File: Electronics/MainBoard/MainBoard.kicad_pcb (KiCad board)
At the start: 2 copper layers, 25 parts, among them CN1 RCable_Con_Front, CN2 RCable_Con_Front, CN3 RCable_Con_VEST, M1 Vibr_Motor, Q1 Q_PNP_CBE, SW1 SW_PUSH, SW2 SPST, U1 LT1004_1.2V

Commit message: First implementation of the eclipse code, as well as some slight further changes to the electronics board.
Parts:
- added D3: D, Discret:R1, F.Cu at (123.2, 106.0)
- R1: value 50KΩ -> 47KΩ
- R2: value 14Ω -> 10Ω
- R7: value 68kΩ -> 47kΩ
- R8: value 33kΩ -> 22kΩ
- moved SP1 86.1 mm to (102.2, 83.2), turned to 0 degrees
- moved R4 63.8 mm to (72.4, 98.4)
- moved R3 63.6 mm to (72.4, 94.6)
- moved BT1 63.5 mm to (118.1, 111.1), turned to 180 degrees
- moved CN2 63.5 mm to (77.5, 87.0)
- moved Q1 63.5 mm to (72.4, 87.0)
- moved R5 63.5 mm to (72.4, 97.2)
- moved D1 62.3 mm to (67.3, 87.0)
- moved D2 62.3 mm to (67.3, 94.6)
- moved R2 59.7 mm to (71.1, 84.5)
- moved MCU1 52.9 mm to (116.8, 103.5), turned to 90 degrees
- moved SW2 52.7 mm to (122.6, 111.1), turned to 270 degrees
- moved CN1 50.8 mm to (109.2, 101.0)
- moved R6 49.3 mm to (118.1, 106.0), turned to 180 degrees
- moved U1 46.1 mm to (129.5, 90.8), turned to 0 degrees
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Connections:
- SW2 pad 1: Net-(BT1-Pad1) -> Net-(D3-Pad1)

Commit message: Adjusted electronics for new knowledge :3
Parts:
- removed R1: 47KΩ, Discret:R1
- removed U1: LT1004_1.2V, TO_SOT_Packages_THT:TO-92_Inline_Wide
- added C3: C, Capacitors_ThroughHole:CP_Radial_D5.0mm_P2.50mm, F.Cu at (134.6, 90.8)
- added J1: CONN_02X04, Pin_Headers:Pin_Header_Straight_2x04_Pitch2.54mm, F.Cu at (129.5, 85.7)
- added R10: RST, Resistors_ThroughHole:R_Axial_DIN0204_L3.6mm_D1.6mm_P2.54mm_Vertical, F.Cu at (127.0, 90.8)
- added R11: RST, Resistors_ThroughHole:R_Axial_DIN0204_L3.6mm_D1.6mm_P2.54mm_Vertical, F.Cu at (124.5, 93.3)
- added R9: RST, Resistors_ThroughHole:R_Axial_DIN0204_L3.6mm_D1.6mm_P2.54mm_Vertical, F.Cu at (129.2, 93.3)
- added REF**: R_1206, Resistors_SMD:R_1206, B.Cu at (121.4, 89.6)
- added REF**: R_1206, Resistors_SMD:R_1206, B.Cu at (118.8, 113.6)
- added REF**: R_1206, Resistors_SMD:R_1206, B.Cu at (117.1, 90.4)
- added REF**: R_1206, Resistors_SMD:R_1206, B.Cu at (125.6, 99.7)
- added REF**: R_1206, Resistors_SMD:R_1206, B.Cu at (118.3, 93.3)
- added REF**: R_1206, Resistors_SMD:R_1206, B.Cu at (125.9, 108.7)
- added REF**: R_1206, Resistors_SMD:R_1206, B.Cu at (118.2, 100.4)
- moved SP1 15.9 mm to (97.8, 98.4), turned to 270 degrees
- moved R8 10.2 mm to (141.0, 93.3)
- moved CN1 7.62 mm to (109.2, 93.3)
- moved D3 5.82 mm to (118.1, 108.8)
- moved R7 5.08 mm to (141.0, 90.8)
- moved SPI1 5.08 mm to (144.8, 93.3)
- moved CN3 3.59 mm to (154.9, 93.3)
- moved D1 3.17 mm to (67.3, 90.2)
- moved QRZ1 1.39 mm to (138.3, 107.1)
- moved BT1 1.27 mm to (116.8, 111.1), turned to 0 degrees
- moved R4 1.27 mm to (72.4, 99.7)
- moved C2 0.43 mm to (142.7, 111.2)
- turned M1 to 180 degrees
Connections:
- MCU1 pad 13: /IR_IN -> Net-(MCU1-Pad13)
- MCU1 pad 14: Net-(MCU1-Pad14) -> /IR_IN
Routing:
- net /SCL: track 0.00 -> 97.7 mm
- net +3V3: track 0.00 -> 83.1 mm
- net /SDA: track 0.00 -> 68.5 mm
- net /RESET: track 0.00 -> 45.4 mm
- net /BZR: track 0.00 -> 41.1 mm
- net /IR_LED: track 0.00 -> 39.7 mm
- net (no net): track 0.00 -> 35.3 mm
- net /TRG: track 0.00 -> 33.1 mm
- net GND: track 0.00 -> 24.9 mm
- net /IR_IN: track 0.00 -> 22.4 mm
- net Net-(J1-Pad5): track 0.00 -> 17.3 mm
- net /V_SENS: track 0.00 -> 16.2 mm
- net /G_LED: track 0.00 -> 15.9 mm
- net /B_LED: track 0.00 -> 14.9 mm
- net /SCK: track 0.00 -> 14.1 mm
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- added copper zone on B.Cu, net GND

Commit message: Small cleanup of schematic & footprint
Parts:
- removed CN1, CN2: RCable_Con_Front, Pin_Headers:Pin_Header_Straight_2x05
- C3: value C -> 22uF
- R3, R4, R5: value 470Ω -> 220Ω
- moved J1 5.68 mm to (134.6, 83.2), turned to 270 degrees
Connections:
- CN3 pad 4: Net-(CN3-Pad4) -> /MOSI
- CN3 pad 5: Net-(CN3-Pad5) -> /MISO
- CN3 pad 6: Net-(CN3-Pad6) -> /SCK
- D1 pad 2: Net-(D1-Pad2) -> +3V3
- D2 pad 2: Net-(CN2-Pad1) -> GND
- J1 pad 1: /SDA -> /E>A
- J1 pad 4: /SCL -> Net-(J1-Pad4)
- J1 pad 8: /HIT_REC -> /A>E
- MCU1 pad 2: /R_LED -> /E>A
- MCU1 pad 24: Net-(MCU1-Pad24) -> /R_MZL
- MCU1 pad 25: Net-(MCU1-Pad25) -> /G_MZL
- MCU1 pad 26: Net-(MCU1-Pad26) -> /B_MZL
- MCU1 pad 3: /G_LED -> /A>E
- MCU1 pad 4: /B_LED -> Net-(MCU1-Pad4)
- Q1 pad 1: Net-(CN2-Pad1) -> GND
- R3 pad 2: Net-(CN2-Pad4) -> /R_MZL
- R4 pad 2: Net-(CN2-Pad5) -> /G_MZL
- R5 pad 2: Net-(CN2-Pad6) -> /B_MZL
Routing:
- net +3V3: track 83.1 -> 108.8 mm
- net /E>A: track 0.00 -> 23.8 mm
- net /SDA: track 68.5 -> 44.9 mm
- net Net-(J1-Pad6): track 6.13 -> 26.8 mm
- net Net-(J1-Pad5): track 17.3 -> 1.19 mm
- net /G_LED: track 15.9 -> 0.00 mm
- net /A>E: track 0.00 -> 15.9 mm
- net /SCL: track 97.7 -> 82.1 mm
- net Net-(MCU1-Pad4): track 0.00 -> 14.9 mm
- net /B_LED: track 14.9 -> 0.00 mm
- net Net-(J1-Pad3): track 9.72 -> 21.2 mm
- net Net-(MCU1-Pad26): track 8.89 -> 0.00 mm
- net /B_MZL: track 0.00 -> 8.89 mm
- net GND: track 24.9 -> 16.1 mm
- net /R_LED: track 7.95 -> 0.00 mm
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- removed copper zone on B.Cu, net GND

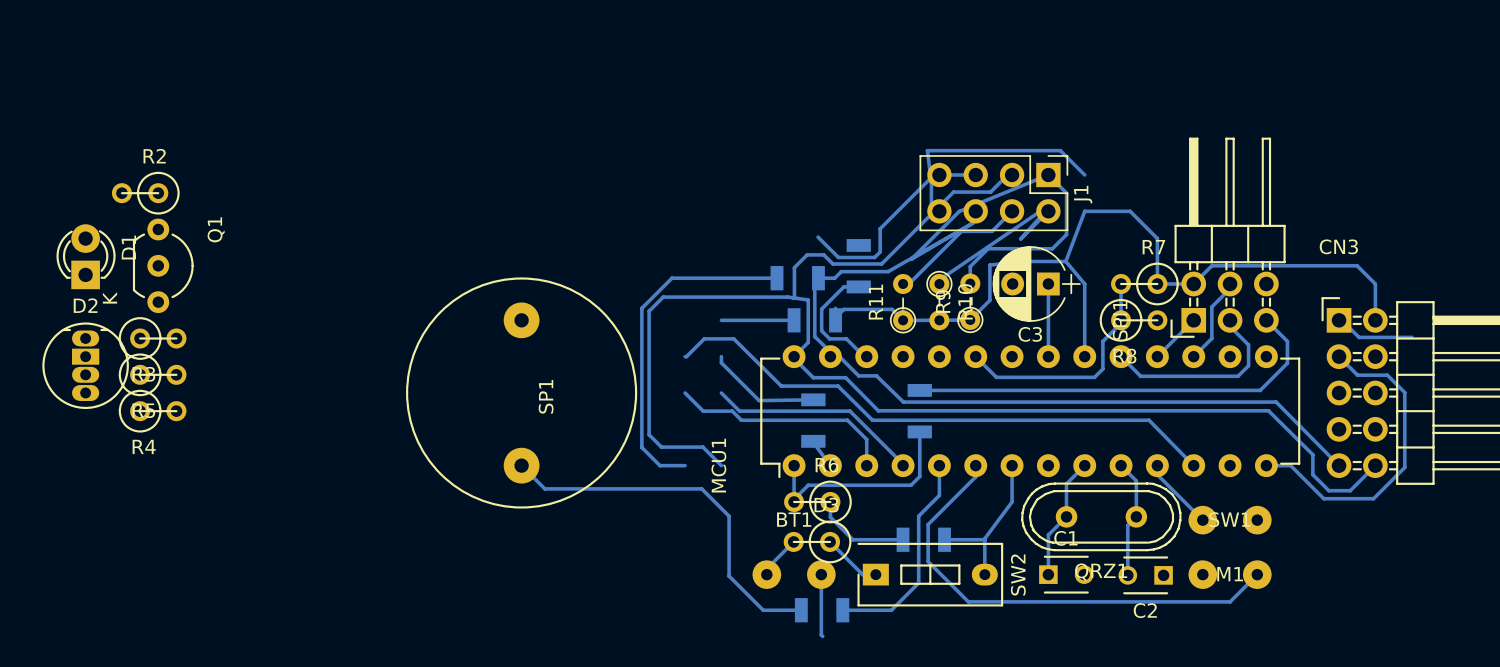
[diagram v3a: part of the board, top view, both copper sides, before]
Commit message: First implement of SMD components
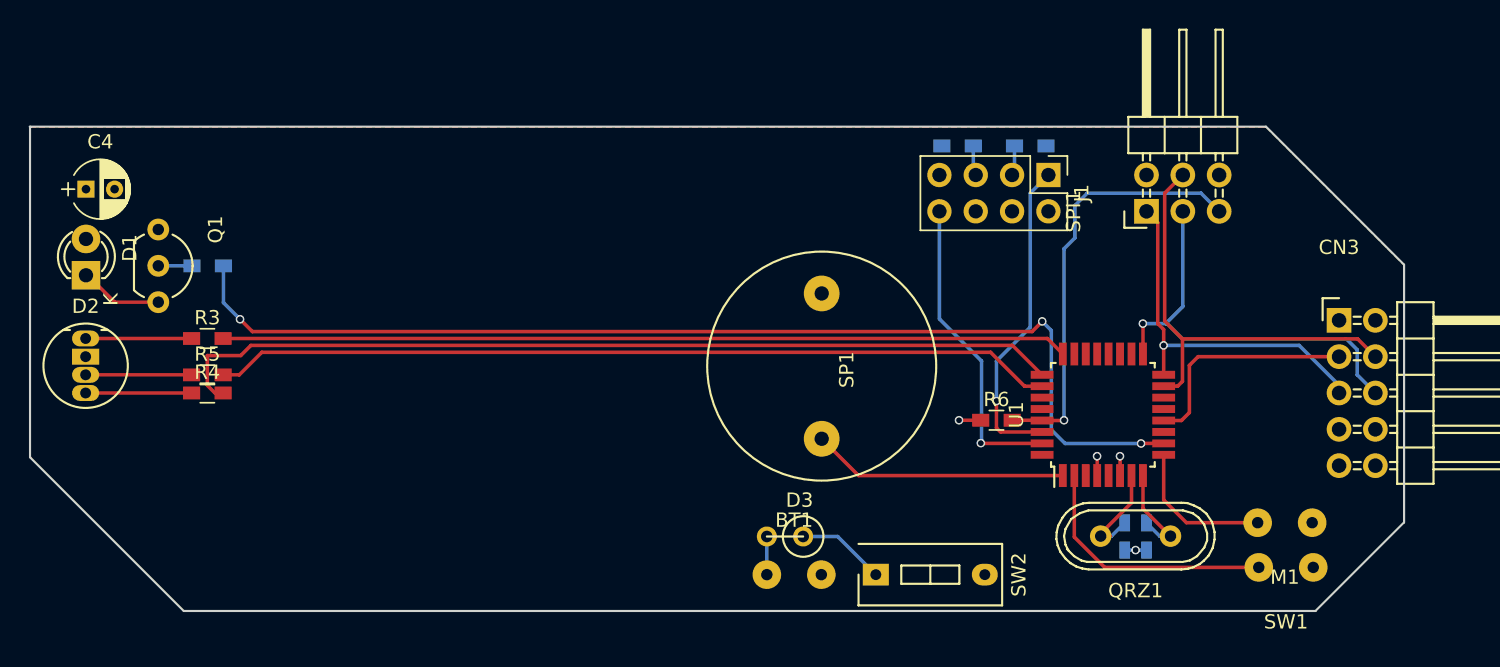
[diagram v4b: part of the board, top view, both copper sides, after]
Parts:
- removed C3: 22uF, Capacitors_ThroughHole:CP_Radial_D5.0mm_P2.50mm
- removed MCU1: ATMEGA328P-P, Housings_DIP:DIP-28_W7.62mm
- removed R10: RST, Resistors_ThroughHole:R_Axial_DIN0204_L3.6mm_D1.6mm_P2.54mm_Vertical
- removed R2: 10Ω, Discret:R1
- removed R7: 47kΩ, Discret:R1
- removed R8: 22kΩ, Discret:R1
- removed REF** (x7): R_1206, Resistors_SMD:R_1206
- added C4: CP, Capacitors_ThroughHole:CP_Radial_D4.0mm_P2.00mm, F.Cu at (67.3, 84.2)
- added R1: 220Ω, Resistors_SMD:R_0603_HandSoldering, B.Cu at (75.8, 89.5)
- added U1: ATMEGA168PA-AU, Housings_QFP:TQFP-32_7x7mm_Pitch0.8mm, F.Cu at (138.4, 99.9)
- C1, C2: footprint Capacitors_ThroughHole:C_Disc_D3_P2.5 -> Capacitors_SMD:C_0603_HandSoldering; moved to B.Cu
- R11, R9: footprint Resistors_ThroughHole:R_Axial_DIN0204_L3.6mm_D1.6mm_P2.54mm_Vertical -> Resistors_SMD:R_0603_HandSoldering; moved to B.Cu
- R3, R4, R5, R6: footprint Discret:R1 -> Resistors_SMD:R_0603_HandSoldering
- moved SP1 21.1 mm to (118.8, 96.5)
- moved R11 15.1 mm to (133.3, 81.2), turned to 180 degrees
- moved R6 14.1 mm to (131.0, 100.3), turned to 0 degrees
- moved R9 12.2 mm to (128.3, 81.2), turned to 0 degrees
- moved SPI1 8.30 mm to (141.5, 85.7)
- moved C1 5.96 mm to (140.0, 108.5), turned to 270 degrees
- moved SW1 3.94 mm to (151.2, 110.6), turned to 180 degrees
- moved M1 3.84 mm to (151.2, 107.5)
- moved R4 3.66 mm to (75.8, 98.4)
- moved R3 3.43 mm to (75.8, 94.6)
- moved R5 3.43 mm to (75.8, 97.2)
- moved C2 2.97 mm to (141.5, 108.5), turned to 90 degrees
- moved QRZ1 2.74 mm to (140.7, 108.4)
- moved D3 1.92 mm to (116.2, 108.5)
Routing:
- net +3V3: track 108.8 -> 4.23 mm, vias 0 -> 3
- net /SCL: track 82.1 -> 0.00 mm
- net /G_MZL: track 0.00 -> 62.9 mm
- net /R_MZL: track 0.00 -> 59.2 mm
- net /B_MZL: track 8.89 -> 58.9 mm
- net /SDA: track 44.9 -> 0.00 mm
- net (no net): track 38.6 -> 0.00 mm
- net /IR_LED: track 39.7 -> 77.0 mm, vias 0 -> 3
- net Net-(J1-Pad6): track 26.8 -> 0.00 mm
- net /MOSI: track 6.13 -> 30.9 mm
- net /BZR: track 41.1 -> 17.9 mm
- net /MISO: track 3.59 -> 25.9 mm, vias 0 -> 1
- net Net-(J1-Pad3): track 21.2 -> 2.10 mm
- net /V_SENS: track 16.2 -> 0.00 mm
- net /SCK: track 14.1 -> 29.8 mm, vias 0 -> 1
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- added copper zone on B.Cu, net +3V3
- added copper zone on F.Cu, net GND
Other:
- board outline added: 96.1 x 33.9 mm

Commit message: More SMD additions
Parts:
- removed BT1: Battery, Main-Cache:SolderWirePad_2x_0-8mmDrill
- removed CN3: RCable_Con_VEST, Pin_Headers:Pin_Header_Angled_2x05
- removed D3: D, Discret:R1
- removed R3, R4, R5: 220Ω, Resistors_SMD:R_0603_HandSoldering
- removed SW2: SPST, Buttons_Switches_ThroughHole:SW_DIP_x1_Slide
- added D4: LED_RGBA, LEDs:LED_Cree-PLCC4_3.2x2.8mm_CCW, F.Cu at (132.0, 93.2)
- added D5: LED_RGBA, LEDs:LED_Cree-PLCC4_3.2x2.8mm_CCW, B.Cu at (132.0, 93.2)
- added J2: DB9_Female, Connectors_DSub:DSUB-9_Female_Horizontal_Pitch2.77x2.84mm_EdgePinOffset4.94mm_Housed_MountingHolesOffset7.48mm, F.Cu at (163.2, 87.6)
- added Q2: 2N 2222A, TO_SOT_Packages_SMD:SOT-23_Handsoldering, F.Cu at (156.8, 97.2)
- added Q3: 2N 2222A, TO_SOT_Packages_SMD:SOT-23_Handsoldering, F.Cu at (156.8, 93.3)
- added Q4: 2N 2222A, TO_SOT_Packages_SMD:SOT-23_Handsoldering, F.Cu at (156.8, 89.5)
- added RN1: 220Ω, Resistors_SMD:R_Array_Convex_4x1206, B.Cu at (134.6, 86.6)
- added RN2: 100Ω, Resistors_SMD:R_Array_Convex_4x1206, B.Cu at (157.0, 93.5)
- added RN3: 220Ω, Resistors_SMD:R_Array_Convex_4x1206, F.Cu at (151.1, 93.3)
- C4: value CP -> 100uF; footprint Capacitors_ThroughHole:CP_Radial_D4.0mm_P2.00mm -> Capacitors_SMD:CP_Elec_6.3x5.7
- D1: footprint LEDs:LED-3MM -> LEDs:LED_D3.0mm_Horizontal_O1.27mm_Z10.0mm
- D2: footprint LEDs:LED-RGB-5MM_Common_Cathode -> LEDs:LED_D5.0mm-4
- Q1: value Q_PNP_CBE -> 2N 2222A; footprint TO_SOT_Packages_THT:TO-92_Inline_Wide -> TO_SOT_Packages_SMD:SOT-23_Handsoldering
- R1: moved to F.Cu
- SP1: footprint Buzzers_Beepers:BUZZER -> Buzzers_Beepers:Buzzer_15x7.5RM7.6
- SPI1: footprint Pin_Headers:Pin_Header_Angled_2x03 -> Pin_Headers:Pin_Header_Straight_2x03_Pitch2.54mm
- moved Q1 135.7 mm to (193.1, 149.0), turned to 0 degrees
- moved R1 114.3 mm to (173.7, 148.7), turned to 0 degrees
- moved C4 57.9 mm to (123.8, 96.9)
- moved R6 47.0 mm to (167.9, 71.2), turned to 270 degrees
- moved D1 39.9 mm to (88.9, 123.8), turned to 0 degrees
- moved D2 32.4 mm to (79.2, 124.7)
- moved SP1 15.0 mm to (121.9, 81.9)
- moved R11 13.0 mm to (146.3, 79.9), turned to 90 degrees
- moved J1 10.3 mm to (144.1, 79.4)
- moved SPI1 9.79 mm to (150.5, 81.9)
- moved U1 6.87 mm to (140.3, 93.3), turned to 45 degrees
- moved R9 6.23 mm to (134.4, 79.9), turned to 90 degrees
- moved QRZ1 6.16 mm to (145.7, 104.8)
- moved SW1 5.18 mm to (153.7, 106.0)
- moved M1 4.71 mm to (153.7, 103.5)
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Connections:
- Q1 pad 1: GND -> Net-(Q1-Pad1)
- Q1 pad 2: Net-(Q1-Pad2) -> GND
- R1 pad 1: /IR_LED -> Net-(R1-Pad1)
- R1 pad 2: Net-(Q1-Pad2) -> Net-(Q1-Pad1)
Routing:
- net /IR_LED: track 77.0 -> 16.8 mm, vias 3 -> 1
- net /G_MZL: track 62.9 -> 3.75 mm, vias 0 -> 1
- net /B_MZL: track 58.9 -> 3.37 mm, vias 0 -> 1
- net /R_MZL: track 59.2 -> 6.30 mm, vias 0 -> 1
- net /SCL: track 0.00 -> 35.2 mm, vias 0 -> 1
- net /SDA: track 0.00 -> 31.9 mm, vias 0 -> 1
- net +3V3: track 4.23 -> 34.8 mm, vias 3 -> 1
- net Net-(D4-Pad1): track 0.00 -> 28.8 mm, vias 0 -> 1
- net Net-(D4-Pad3): track 0.00 -> 27.3 mm, vias 0 -> 1
- net Net-(D4-Pad2): track 0.00 -> 27.3 mm, vias 0 -> 1
- net /R_PWR: track 0.00 -> 15.1 mm, vias 0 -> 1
- net GND: track 1.53 -> 14.4 mm
- net /B_PWR: track 0.00 -> 12.1 mm, vias 0 -> 1
- net /A>E: track 21.7 -> 11.1 mm, vias 1 -> 0
- net /IR_IN: track 16.0 -> 26.4 mm, vias 0 -> 1
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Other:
- board size 96.1 x 33.9 mm -> 103.5 x 31.1 mm

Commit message: Final small changes
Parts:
- added BT1: Battery, Connectors_JST:JST_PH_S2B-PH-K_02x2.00mm_Angled, F.Cu at (132.5, 102.3)
- added Q5: 2N 2222A, TO_SOT_Packages_SMD:SOT-23_Handsoldering, F.Cu at (154.1, 100.6)
- added SW2: SPST, Pin_Headers:Pin_Header_Straight_1x03_Pitch2.54mm, F.Cu at (128.7, 107.3)
- C4: value 100uF -> 22uF; footprint Capacitors_SMD:CP_Elec_6.3x5.7 -> Capacitors_SMD:CP_Elec_5x5.3
- Q1, R6: moved to B.Cu
- R1: value 220Ω -> 470Ω
- moved Q1 92.0 mm to (126.4, 85.6), turned to 180 degrees
- moved R1 54.8 mm to (149.2, 99.7), turned to 180 degrees
- moved D2 44.0 mm to (117.5, 102.9), turned to 270 degrees
- moved D1 38.7 mm to (117.5, 97.8), turned to 270 degrees
- moved R6 13.8 mm to (157.7, 80.5)
- moved C4 7.79 mm to (124.6, 104.6), turned to 90 degrees
- moved D4 1.14 mm to (130.8, 93.2)
- moved D5 1.14 mm to (130.8, 93.2)
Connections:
- C4 pad 1: +3V3 -> Net-(BT1-Pad1)
- J2 pad 5: Net-(J2-Pad5) -> /V_VBR
- M1 pad 1: GND -> Net-(M1-Pad1)
- M1 pad 2: /VBR -> +3V3
- R1 pad 1: Net-(R1-Pad1) -> Net-(Q5-Pad1)
- R1 pad 2: Net-(Q1-Pad1) -> /VBR
- RN1 pad 8: Net-(R1-Pad1) -> Net-(Q1-Pad1)
- U1 pad 11: Net-(U1-Pad11) -> /V_VBR
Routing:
- net Net-(D2-Pad3): track 0.00 -> 28.4 mm
- net Net-(D2-Pad4): track 0.00 -> 28.4 mm
- net Net-(D2-Pad1): track 0.00 -> 24.2 mm, vias 0 -> 1
- net /V_VBR: track 0.00 -> 22.5 mm, vias 0 -> 1
- net GND: track 14.4 -> 36.3 mm, vias 1 -> 2
- net Net-(D1-Pad1): track 0.00 -> 17.6 mm
- net Net-(BT1-Pad1): track 0.00 -> 11.8 mm
- net +3V3: track 34.8 -> 43.0 mm, vias 1 -> 3
- net Net-(Q1-Pad1): track 0.00 -> 5.22 mm
- net /VBR: track 12.5 -> 8.76 mm
- net Net-(M1-Pad1): track 0.00 -> 2.93 mm
- net /RESET: track 27.3 -> 29.6 mm
- net Net-(Q5-Pad1): track 0.00 -> 2.25 mm
- net Net-(D4-Pad3): track 27.3 -> 28.7 mm
- net Net-(D4-Pad1): track 28.8 -> 30.0 mm

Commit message: Finalized schematics and Gerbers - for now
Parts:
- added REF***: OSHW-Logo2_9.8x8mm_Copper, Symbols:OSHW-Logo2_9.8x8mm_Copper, F.Cu at (125.5, 96.8)
- BT1: footprint Connectors_JST:JST_PH_S2B-PH-K_02x2.00mm_Angled -> Connectors_JST:JST_PH_B2B-PH-K_02x2.00mm_Straight
- M1, SW1: footprint Main-Cache:SolderWirePad_2x_0-8mmDrill -> Pin_Headers:Pin_Header_Straight_1x02_Pitch2.54mm
- QRZ1: value Crystal_Small -> 4MHz
- RN1, RN3: footprint Resistors_SMD:R_Array_Convex_4x1206 -> Resistors_SMD:R_Array_Convex_4x0603
- RN2: value 100Ω -> 220Ω; footprint Resistors_SMD:R_Array_Convex_4x1206 -> Resistors_SMD:R_Array_Convex_4x0603
- moved BT1 2.45 mm to (132.7, 104.8)
- moved M1 1.91 mm to (155.6, 103.5), turned to 270 degrees
- moved SW1 1.91 mm to (155.6, 106.0), turned to 270 degrees
- moved RN3 1.55 mm to (151.4, 91.8)
- moved RN1 0.83 mm to (134.2, 85.9)
- moved RN2 0.51 mm to (157.0, 93.0)
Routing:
- net /SCK: track 21.9 -> 26.7 mm, vias 0 -> 2
- net /MISO: track 23.1 -> 18.5 mm
- net Net-(BT1-Pad1): track 11.8 -> 8.88 mm
- net Net-(D2-Pad1): track 24.2 -> 27.0 mm
- net Net-(D2-Pad4): track 28.4 -> 30.5 mm
- net /MOSI: track 30.7 -> 28.7 mm
- net Net-(Q2-Pad1): track 4.37 -> 6.35 mm
- net /G_MZL: track 3.75 -> 5.67 mm
- net Net-(D2-Pad3): track 28.4 -> 29.9 mm
- net GND: track 36.3 -> 37.8 mm
- net /TRG: track 25.9 -> 27.2 mm
- net /IR_LED: track 16.8 -> 18.0 mm
- net /R_MZL: track 6.30 -> 7.49 mm
- net /B_MZL: track 3.37 -> 4.47 mm
- net Net-(Q3-Pad1): track 2.84 -> 3.87 mm
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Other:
- board size 103.5 x 31.1 mm -> 57.8 x 31.1 mm
- net class Default: via_dia 0.6 -> 0.72; via_drill 0.4 -> 0.52
